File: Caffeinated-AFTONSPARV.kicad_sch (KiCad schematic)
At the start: 12 parts, among them J1 Conn_01x02, J2 Conn_01x04, Q1 AO3400A, Q2 AO3400A, Q3 AO3400A, SW1 SW_Push

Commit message: feat(): Finalize design
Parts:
- added C22: 100µF 35V, Capacitor_THT:CP_Radial_D6.3mm_P2.50mm, symbol Device:C_Polarized
- added C5 (x2): 100nF, Capacitor_SMD:C_0603_1608Metric, symbol Device:C
- added C5: 4.7uF, Capacitor_SMD:C_0805_2012Metric, symbol Device:C
- added C5 (x2): 22uF, Capacitor_SMD:C_0603_1608Metric, symbol Device:C
- added J3: TagConnect, Connector:Tag-Connect_TC2030-IDC-NL_2x03_P1.27mm_Vertical, symbol caffeinated-labs:Tag-Connect-ESP
- added L1: 10uH, PCM_Inductor_SMD_AKL:L_1206_3216Metric, symbol Device:L
- added R10, R12, R14, R7, R8, R9: 10k, Resistor_SMD:R_0603_1608Metric, symbol Device:R
- added R11: 1, Resistor_SMD:R_0603_1608Metric, symbol Device:R
- added R13: 18k, Resistor_SMD:R_0603_1608Metric, symbol Device:R
- added U1: ESP32-C3-MINI-1, PCM_Espressif:ESP32-C3-MINI-1, symbol PCM_Espressif:ESP32-C3-MINI-1
- added U2: SY8201ABC, Package_TO_SOT_SMD:SOT-23-6, symbol caffeinated-labs:SY8201
- Q1, Q2, Q3: footprint Package_TO_SOT_SMD_AKL:SOT-23 -> Package_TO_SOT_SMD:SOT-23
- R1, R2, R3, R4, R5, R6: footprint (none) -> Resistor_SMD:R_0603_1608Metric
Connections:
- net +24V: now also C22.1, C5.1, R11.1
- net GND: now also SW1.1, C22.2, C5.1, C5.2, C5.2, J3.5 (GND), R13.2, U1.1 (GND), U1.11 (GND), U1.14 (GND), U1.2 (GND), U1.36 (GND), U1.37 (GND), U1.38 (GND), U1.39 (GND), U1.40 (GND), U1.41 (GND), U1.42 (GND), U1.43 (GND), U1.44 (GND), U1.45 (GND), U1.46 (GND), U1.47 (GND), U1.48 (GND), U1.49 (GND), U1.50 (GND), U1.51 (GND), U1.52 (GND), U1.53 (GND), U2.2 (GND)
- net at SW1.2: now also J3.2 (IO0/IO8), R7.2, U1.23 (GPIO9)
- net at R2.1, R4.1: now also U1.19 (GPIO5/ADC2_CH0)
- net at R3.1, R6.1: now also U1.20 (GPIO6)
- net at R1.1, R5.1: now also U1.18 (GPIO4/ADC1_CH4)
- new net: C5.1, L1.1, U2.6 (LX)
- new net: C5.2, U2.1 (BS)
- new net: C5.1, R11.2, R14.1, U2.5 (IN)
- new net: R9.2, U1.22 (GPIO8)
- new net: J3.4 (RX), U1.30 (GPIO20/U0RXD)
- new net: J3.3 (TX), U1.31 (GPIO21/U0TXD)
- new net: R8.2, U1.5 (GPIO2/ADC1_CH2)
- new net: J3.6 (EN), R10.2, U1.8 (EN/CHIP_PU)
- new net: C5.1, R12.2, R13.1, U2.3 (FB)
- new net: R14.2, U2.4 (EN)
- new net +3.3V: C5.2, C5.2, J3.1 (VCC), L1.2, R10.1, R12.1, R7.1, R8.1, R9.1, U1.3 (3V3)
- no-connect marks 0 -> 7
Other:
- moved on the sheet: R1, R2, R3, SW1

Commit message: feat(): Rework pcb to 4 layers
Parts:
- added C5: 100uF, Capacitor_SMD:C_0603_1608Metric, symbol Device:C
- added C5: 100nF, Capacitor_SMD:C_0603_1608Metric, symbol Device:C
- added FB1: FerriteBead, PCM_Ferrite_SMD_AKL:Ferrite_0603_1608Metric, symbol Device:FerriteBead
- C5: value 22uF -> 22pF
- R12: value 10k -> 100k
- R13: value 18k -> 22,1k
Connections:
- net +3.3V: now also FB1.2; no longer U1.3 (3V3)
- net GND: now also C5.2, C5.2
- new net: C5.1, C5.1, FB1.1, U1.3 (3V3)
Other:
- note added: "C as np0 and tantal"
- note added: "Validate R"
- moved on the sheet: C5

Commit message: feat(): Rework and finalize design
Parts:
- removed C5: 100uF, Capacitor_SMD:C_0603_1608Metric, symbol Device:C
- removed C5: 22uF, Capacitor_SMD:C_0603_1608Metric, symbol Device:C
- removed FB1: FerriteBead, PCM_Ferrite_SMD_AKL:Ferrite_0603_1608Metric, symbol Device:FerriteBead
- added C5: 100nF, Capacitor_SMD:C_0603_1608Metric, symbol Device:C
- added C5 (x3): 4.7uF, Capacitor_SMD:C_0805_2012Metric, symbol Device:C
- added J4: USB, Connector_PinSocket_1.00mm:PinSocket_1x04_P1.00mm_Vertical, symbol Connector_Generic:Conn_01x04
- C22: LCSC C19702 -> (none)
- C5: LCSC C14663 -> (none)
- J1: value Conn_01x02 -> PWR; now left out of the parts list
- J2: value Conn_01x04 -> LED; now left out of the parts list
- J3: now left out of the parts list
- Q1, Q2, Q3: LCSC (none) -> C347475
- R1, R10, R14, R2, R3, R7, R8, R9: value 10k -> 10kΩ
- R11: value 1 -> 1Ω
- R12: value 100k -> 100kΩ
- R13: value 22,1k -> 22.1kΩ
- R4, R5, R6: value 470 -> 20Ω
- SW1: footprint Button_Switch_SMD:SW_Push_1P1T_XKB_TS-1187A -> caffeinated-labs:YTS-C005; LCSC (none) -> C318884
- U1: value ESP32-C3-MINI-1 -> ESP32-C3-MINI-1-[H/N]4; LCSC (none) -> C2934569 / C2838502
- U2: LCSC (none) -> C108052
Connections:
- net +3.3V: now also C5.1, U1.3 (3V3), C5.1, C5.1, C5.1, C5.1, J4.4 (Pin_4)
- net GND: now also C5.2, C5.2, C5.2, C5.2, J4.1 (Pin_1)
- net IO9: now reaches J3.2 (IO0/IO9), R7.2, SW1.2, U1.23 (GPIO9)
- net LED-B: now reaches R1.1, R5.1
- net LED-B: now also U1.20 (GPIO6); no longer U1.18 (GPIO4/ADC1_CH4)
- net LED-G: now reaches R2.1, R4.1, U1.19 (GPIO5/ADC2_CH0)
- net LED-R: now reaches R3.1, R6.1
- net LED-R: now also U1.18 (GPIO4/ADC1_CH4); no longer U1.20 (GPIO6)
- net USB-D-: now reaches U1.26 (GPIO18/USB_D-)
- net USB-D-: now also J4.3 (Pin_3)
- net USB-D+: now reaches U1.27 (GPIO19/USB_D+)
- net USB-D+: now also J4.2 (Pin_2)
- net RX: now reaches J3.4 (RX), U1.30 (GPIO20/U0RXD)
- net TX: now reaches J3.3 (TX), U1.31 (GPIO21/U0TXD)
- net EN: now reaches J3.6 (EN), R10.2, U1.8 (EN/CHIP_PU)
- no-connect marks 7 -> 5
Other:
- note removed: "C as np0 and tantal"
- note removed: "Validate R"
- moved on the sheet: C22, C5, J1, J2, J3, L1, Q1, Q2, Q3, R1, R10, R11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

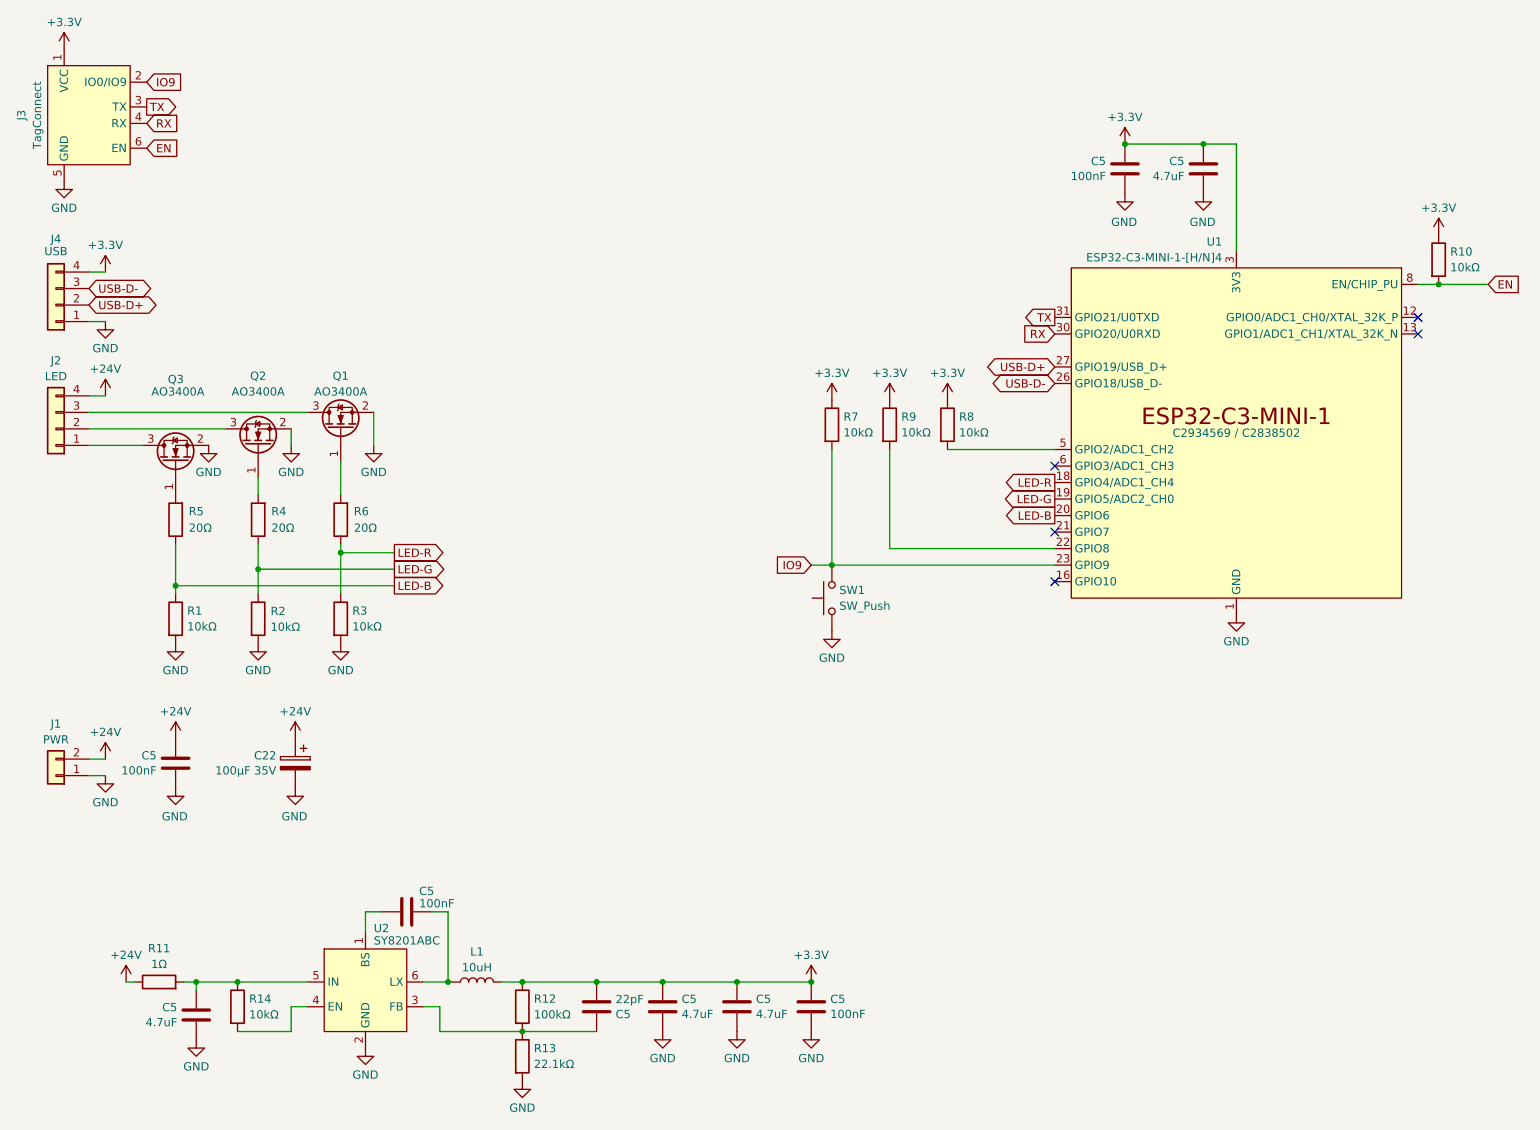
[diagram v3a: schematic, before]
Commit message: feat(): Replace L1 footprint and add Refs
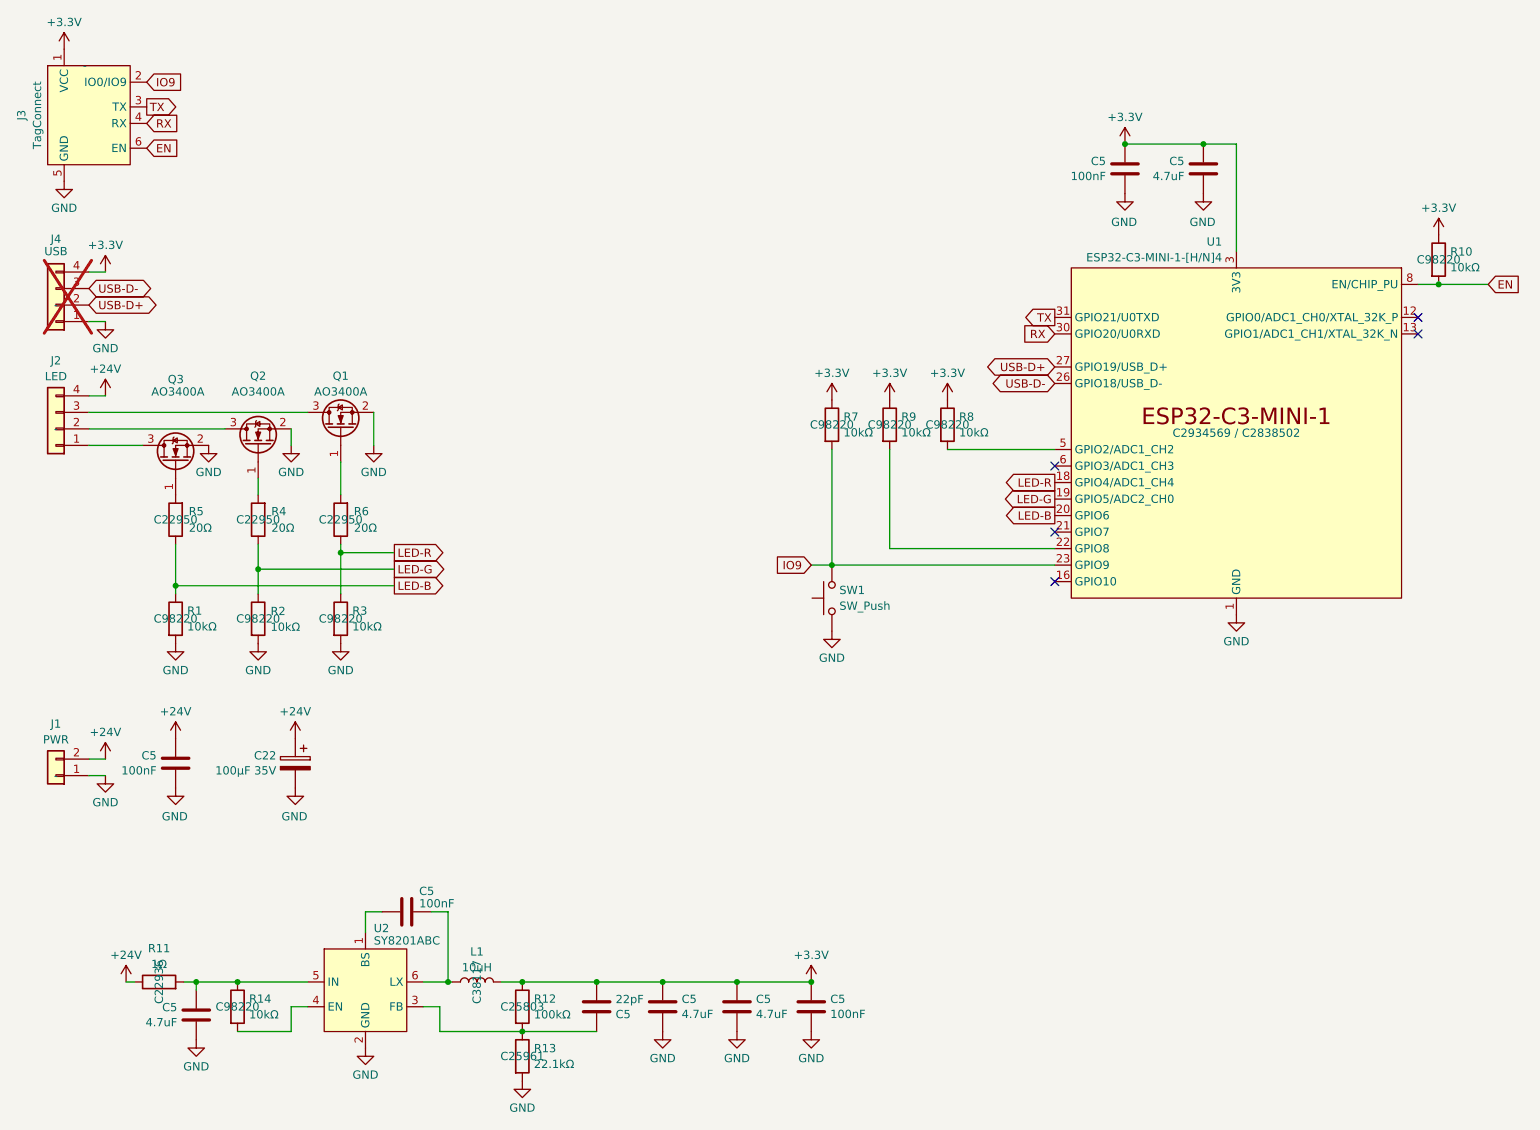
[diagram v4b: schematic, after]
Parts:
- C22: LCSC (none) -> C2831717
- C5: LCSC C14663 -> C560882
- C5: LCSC (none) -> C105620
- J1, J2, J3: LCSC (none) -> -
- J4: LCSC (none) -> -; now not fitted; now left out of the parts list
- L1: footprint PCM_Inductor_SMD_AKL:L_1206_3216Metric -> Inductor_SMD:L_Sunlord_SWPA4030S; LCSC (none) -> C38117
- R1, R10, R14, R2, R3, R7, R8, R9: LCSC (none) -> C98220
- R11: LCSC (none) -> C22936
- R12: LCSC (none) -> C25803
- R13: LCSC (none) -> C25961
- R4, R5, R6: LCSC (none) -> C22950
- SW1: LCSC C318884 -> C2910751
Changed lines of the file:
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@@
       (effects (font (size 1.27 1.27)) hide)
     )
-    (property "Datasheet" "~" (at 134.62 111.125 0)
-      (effects (font (size 1.27 1.27)) hide)
-    )
-    (property "LCSC" "C318884" (at 139.7 111.125 0)
+    (property "Datasheet" "https://datasheet.lcsc.com/lcsc/2111221830_YIYUAN-YTS-C005-2H_C2910751.pdf" (at 134.62 111.125 0)
+      (effects (font (size 1.27 1.27)) hide)
+    )
+    (property "LCSC" "C2910751" (at 139.7 111.125 0)
       (effects (font (size 1.27 1.27)) hide)
     )
@@
       (effects (font (size 1.27 1.27)) hide)
     )
-    (property "LCSC" "C14663" (at 196.85 45.085 0)
+    (property "LCSC" "C560882" (at 196.85 45.085 0)
       (effects (font (size 1.27 1.27)) hide)
     )
@@
       (effects (font (size 1.27 1.27)) hide)
     )
-    (property "LCSC" "" (at 57.15 136.525 0)
+    (property "LCSC" "C2831717" (at 57.15 136.525 0)
       (effects (font (size 1.27 1.27)) hide)
     )
@@
       (effects (font (size 1.27 1.27)) hide)
     )
-    (property "LCSC" "" (at 20.32 85.09 0)
+    (property "LCSC" "-" (at 20.32 85.09 0)
       (effects (font (size 1.27 1.27)))
     )
@@
       (effects (font (size 1.27 1.27)) hide)
     )
-    (property "LCSC" "" (at 139.7 84.455 0)
+    (property "LCSC" "C98220" (at 139.7 84.455 0)
       (effects (font (size 1.27 1.27)))
     )
@@
       (effects (font (size 1.27 1.27)) hide)
     )
-    (property "LCSC" "" (at 20.32 138.43 0)
+    (property "LCSC" "-" (at 20.32 138.43 0)
       (effects (font (size 1.27 1.27)))
     )
@@
       (effects (font (size 1.27 1.27)) hide)
     )
-    (property "LCSC" "C14663" (at 41.91 175.26 0)
+    (property "LCSC" "C560882" (at 41.91 175.26 0)
       (effects (font (size 1.27 1.27)) hide)
     )
@@
       (effects (font (size 1.27 1.27)))
     )
-    (property "Footprint" "PCM_Inductor_SMD_AKL:L_1206_3216Metric" (at 85.09 170.18 0)
+    (property "Footprint" "Inductor_SMD:L_Sunlord_SWPA4030S" (at 85.09 170.18 0)
       (effects (font (size 1.27 1.27)) hide)
     )
@@
       (effects (font (size 1.27 1.27)) hide)
     )
-    (property "LCSC" "" (at 85.09 170.18 0)
+    (property "LCSC" "C38117" (at 85.09 170.18 0)
       (effects (font (size 1.27 1.27)))
     )
@@
       (effects (font (size 1.27 1.27)) hide)
     )
-    (property "LCSC" "" (at 51.435 114.3 0)
+    (property "LCSC" "C98220" (at 51.435 114.3 0)
       (effects (font (size 1.27 1.27)))
     )
@@
       (effects (font (size 1.27 1.27)) hide)
     )
-    (property "LCSC" "" (at 64.135 114.3 0)
+    (property "LCSC" "C98220" (at 64.135 114.3 0)
       (effects (font (size 1.27 1.27)))
     )
@@
       (effects (font (size 1.27 1.27)) hide)
     )
-    (property "LCSC" "" (at 38.735 99.06 0)
+    (property "LCSC" "C22950" (at 38.735 99.06 0)
       (effects (font (size 1.27 1.27)))
     )
@@
       (effects (font (size 1.27 1.27)) hide)
     )
-    (property "LCSC" "" (at 103.505 173.99 0)
+    (property "LCSC" "C105620" (at 103.505 173.99 0)
       (effects (font (size 1.27 1.27)) hide)
     )
@@
       (effects (font (size 1.27 1.27)) hide)
     )
-    (property "LCSC" "" (at 157.48 84.455 0)
+    (property "LCSC" "C98220" (at 157.48 84.455 0)
       (effects (font (size 1.27 1.27)))
     )
@@
       (effects (font (size 1.27 1.27)) hide)
     )
-    (property "LCSC" "" (at 51.435 99.06 0)
+    (property "LCSC" "C22950" (at 51.435 99.06 0)
       (effects (font (size 1.27 1.27)))
     )
@@
       (effects (font (size 1.27 1.27)) hide)
     )
-    (property "LCSC" "C14663" (at 113.665 173.99 0)
+    (property "LCSC" "C560882" (at 113.665 173.99 0)
       (effects (font (size 1.27 1.27)) hide)
     )
@@
       (effects (font (size 1.27 1.27)) hide)
     )
-    (property "LCSC" "" (at 92.075 173.99 0)
+    (property "LCSC" "C25803" (at 92.075 173.99 0)
       (effects (font (size 1.27 1.27)))
     )
@@
       (effects (font (size 1.27 1.27)) hide)
     )
-    (property "LCSC" "C14663" (at 125.095 173.99 0)
+    (property "LCSC" "C560882" (at 125.095 173.99 0)
       (effects (font (size 1.27 1.27)) hide)
     )
@@
       (effects (font (size 1.27 1.27)) hide)
     )
-    (property "LCSC" "" (at 36.195 170.18 0)
+    (property "LCSC" "C22936" (at 36.195 170.18 0)
       (effects (font (size 1.27 1.27)))
     )
@@
       (effects (font (size 1.27 1.27)) hide)
     )
-    (property "LCSC" "" (at 64.135 99.06 0)
+    (property "LCSC" "C22950" (at 64.135 99.06 0)
       (effects (font (size 1.27 1.27)))
     )
@@
       (effects (font (size 1.27 1.27)) hide)
     )
-    (property "LCSC" "" (at 48.26 173.99 0)
+    (property "LCSC" "C98220" (at 48.26 173.99 0)
       (effects (font (size 1.27 1.27)))
     )
@@
   )
   (symbol (lib_id "Connector_Generic:Conn_01x04") (at 20.32 66.04 180) (unit 1)
-    (in_bom yes) (on_board yes) (dnp no)
+    (in_bom no) (on_board yes) (dnp yes)
     (property "Reference" "J4" (at 20.32 55.88 0)
       (effects (font (size 1.27 1.27)))
@@
       (effects (font (size 1.27 1.27)) hide)
     )
-    (property "LCSC" "" (at 20.32 66.04 0)
+    (property "LCSC" "-" (at 20.32 66.04 0)
       (effects (font (size 1.27 1.27)))
     )
@@
       (effects (font (size 1.27 1.27)) hide)
     )
-    (property "LCSC" "" (at 148.59 84.455 0)
+    (property "LCSC" "C98220" (at 148.59 84.455 0)
       (effects (font (size 1.27 1.27)))
     )
@@
       (effects (font (size 1.27 1.27)) hide)
     )
-    (property "LCSC" "" (at 38.735 114.3 0)
+    (property "LCSC" "C98220" (at 38.735 114.3 0)
       (effects (font (size 1.27 1.27)))
     )
@@
       (effects (font (size 1.27 1.27)) hide)
     )
-    (property "LCSC" "" (at 92.075 181.61 0)
+    (property "LCSC" "C25961" (at 92.075 181.61 0)
       (effects (font (size 1.27 1.27)))
     )
@@
       (effects (font (size 1.27 1.27)) hide)
     )
-    (property "LCSC" "" (at 24.765 29.21 0)
+    (property "LCSC" "-" (at 24.765 29.21 0)
       (effects (font (size 1.27 1.27)))
     )
@@
       (effects (font (size 1.27 1.27)) hide)
     )
-    (property "LCSC" "" (at 233.045 59.055 0)
-      (effects (font (size 1.27 1.27)))
-    )
+    (property "LCSC" "C98220" (at 233.045 59.055 0)
+      (effects (font (size 1.27 1.27)))
+    )

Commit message: feat(): Update silkscreen, ibom, use smaller sw
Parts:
- SW1: LCSC C2910751 -> C2910748
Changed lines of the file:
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@@
       (effects (font (size 1.27 1.27)) hide)
     )
-    (property "LCSC" "C2910751" (at 139.7 111.125 0)
+    (property "LCSC" "C2910748" (at 139.7 111.125 0)
       (effects (font (size 1.27 1.27)) hide)
     )
